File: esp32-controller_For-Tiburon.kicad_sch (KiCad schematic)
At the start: 7 parts, among them J1 PWR_IN, J2 UART1, J3 UART2, J4 I2C_OLED, J5 I2C_PressureSensor, J6 SD_Card_Receptacle, U1 ESP32-S3-WROOM-1

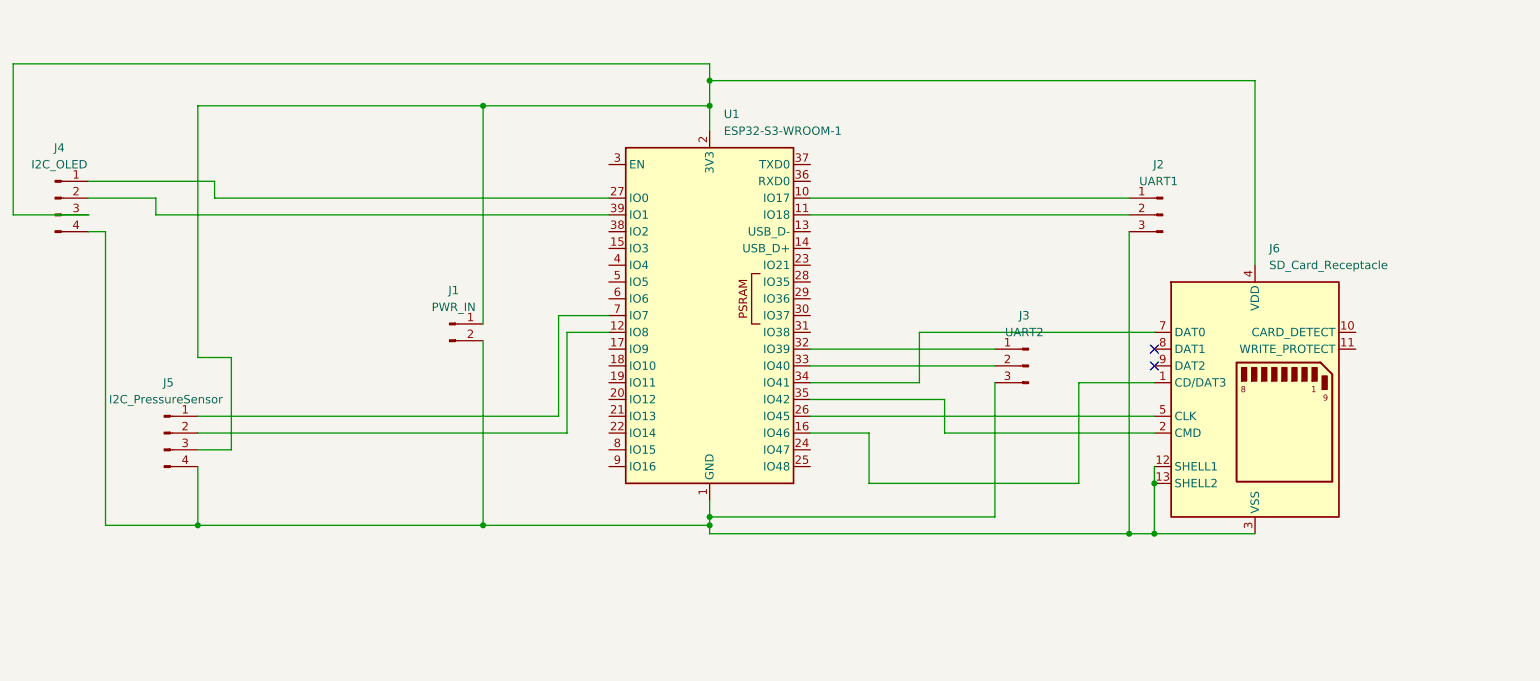
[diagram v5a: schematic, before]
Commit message: added spi2 pins
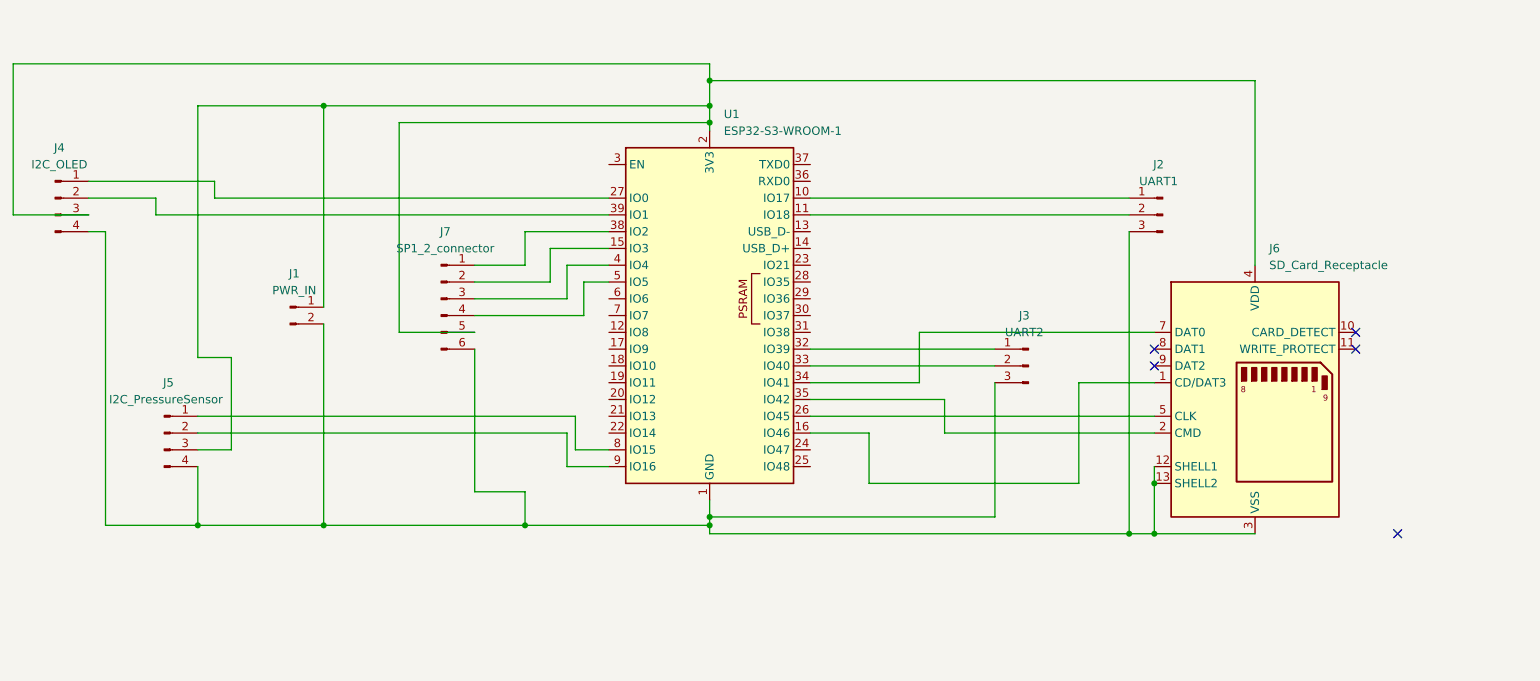
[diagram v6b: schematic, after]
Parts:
- added J7: SP1_2_connector, symbol Connector:Conn_01x06_Pin
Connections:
- net at J1.1 (Pin_1), J4.3 (Pin_3), J5.3 (Pin_3)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: now also J7.5 (Pin_5)
- net at J1.2 (Pin_2), J2.3 (Pin_3), J3.3 (Pin_3)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: now also J7.6 (Pin_6)
- net at U1.12 (IO8): no longer J5.2 (Pin_2)
- net at U1.15 (IO3): now also J7.2 (Pin_2)
- net at U1.38 (IO2): now also J7.1 (Pin_1)
- net at U1.4 (IO4): now also J7.3 (Pin_3)
- net at U1.5 (IO5): now also J7.4 (Pin_4)
- net at U1.7 (IO7): no longer J5.1 (Pin_1)
- net at U1.8 (IO15): now also J5.1 (Pin_1)
- net at U1.9 (IO16): now also J5.2 (Pin_2)
- no-connect marks 2 -> 5
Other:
- moved on the sheet: J1

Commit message: Circuit cleanup
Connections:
- net +3.3V: now reaches J1.1 (Pin_1), J4.3 (Pin_3), J5.3 (Pin_3), J6.4 (VDD), J7.5 (Pin_5), U1.2 (3V3)
- net GND: now reaches J1.2 (Pin_2), J2.3 (Pin_3), J3.3 (Pin_3), J4.4 (Pin_4), J5.4 (Pin_4), J6.12 (SHELL1), J6.13 (SHELL2), J6.3 (VSS), J6.6 (VSS), J7.6 (Pin_6), U1.1 (GND), U1.40 (GND), U1.41 (GND)
- net at J3.1 (Pin_1): now also U1.34 (IO41); no longer U1.32 (IO39)
- net at J3.2 (Pin_2): now also U1.35 (IO42); no longer U1.33 (IO40)
- net at J2.1 (Pin_1): now also U1.32 (IO39); no longer U1.10 (IO17)
- net at J2.2 (Pin_2): now also U1.33 (IO40); no longer U1.11 (IO18)
- net at J7.1 (Pin_1): now also U1.28 (IO35); no longer U1.38 (IO2)
- net at J7.2 (Pin_2): now also U1.29 (IO36); no longer U1.15 (IO3)
- net at J7.3 (Pin_3): now also U1.30 (IO37); no longer U1.4 (IO4)
- net at J7.4 (Pin_4): now also U1.31 (IO38); no longer U1.5 (IO5)
- net at J6.1 (CD/DAT3): now also U1.25 (IO48); no longer U1.16 (IO46)
- net at J6.2 (CMD): now also U1.16 (IO46); no longer U1.35 (IO42)
- net at J6.5 (CLK): now also U1.24 (IO47); no longer U1.26 (IO45)
- net at J6.7 (DAT0): now also U1.26 (IO45); no longer U1.34 (IO41)
- net at U1.21 (IO13): now also J4.1 (Pin_1)
- net at U1.22 (IO14): now also J4.2 (Pin_2)
- net at U1.27 (IO0): no longer J4.1 (Pin_1)
- net at U1.39 (IO1): no longer J4.2 (Pin_2)
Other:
- moved on the sheet: J1, J3, J4, J5, J6, J7

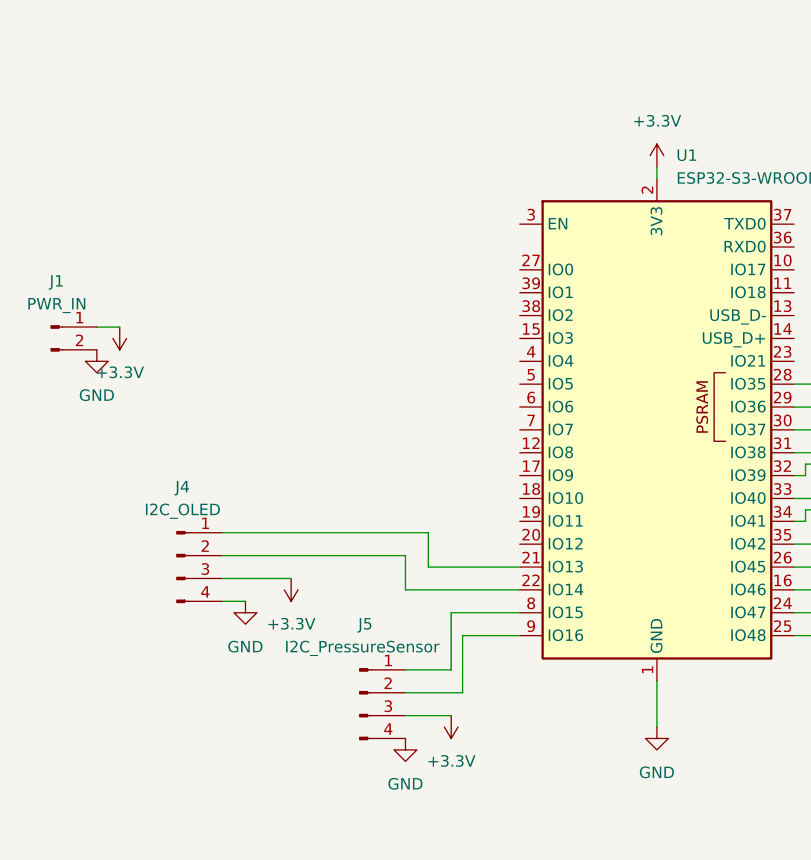
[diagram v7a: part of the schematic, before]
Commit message: Added pullup resistors and capacitors till the i2c protocol
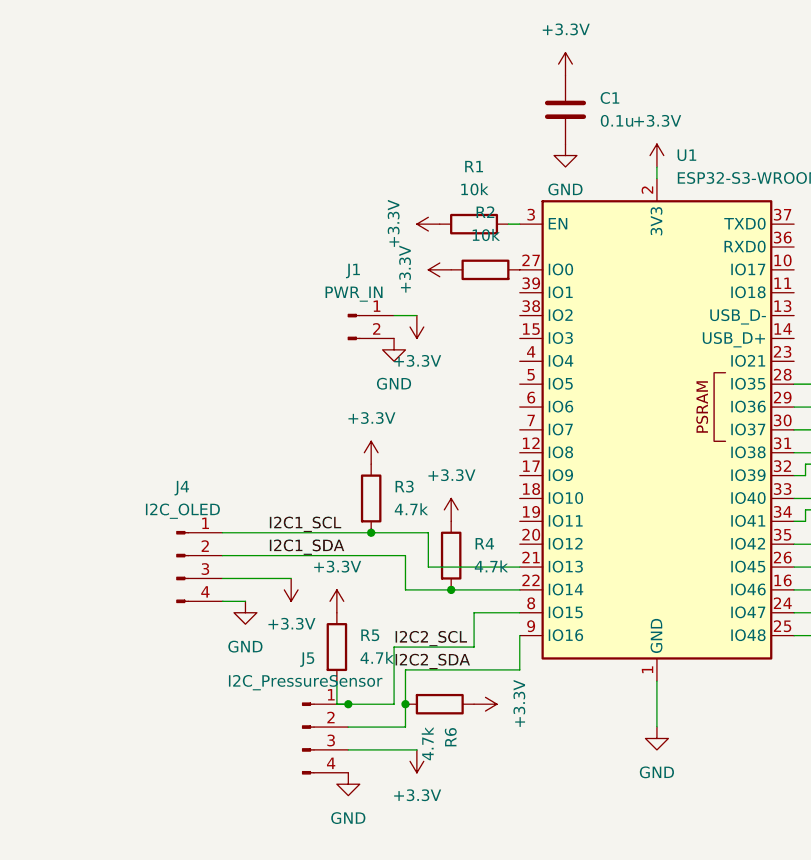
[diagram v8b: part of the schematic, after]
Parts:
- added C1: 0.1u, symbol Device:C
- added R1, R2: 10k, symbol Device:R
- added R3, R4, R5, R6: 4.7k, symbol Device:R
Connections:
- net +3.3V: now also C1.1, R1.1, R2.1, R3.1, R4.1, R5.1, R6.1
- net GND: now also C1.2
- net I2C1_SCL: now reaches J4.1 (Pin_1), U1.21 (IO13)
- net I2C1_SCL: now also R3.2
- net I2C1_SDA: now reaches J4.2 (Pin_2), U1.22 (IO14)
- net I2C1_SDA: now also R4.2
- net at U1.27 (IO0): now also R2.2
- net at U1.3 (EN): now also R1.2
- net I2C2_SCL: now reaches J5.1 (Pin_1), U1.8 (IO15)
- net I2C2_SCL: now also R5.2
- net at J5.2 (Pin_2), U1.9 (IO16): now also R6.2
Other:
- moved on the sheet: J1, J5
